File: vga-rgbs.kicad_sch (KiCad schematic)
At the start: 14 parts, among them J1 VGA, Q1 BC847, Q2 BC847, U1 74LS86

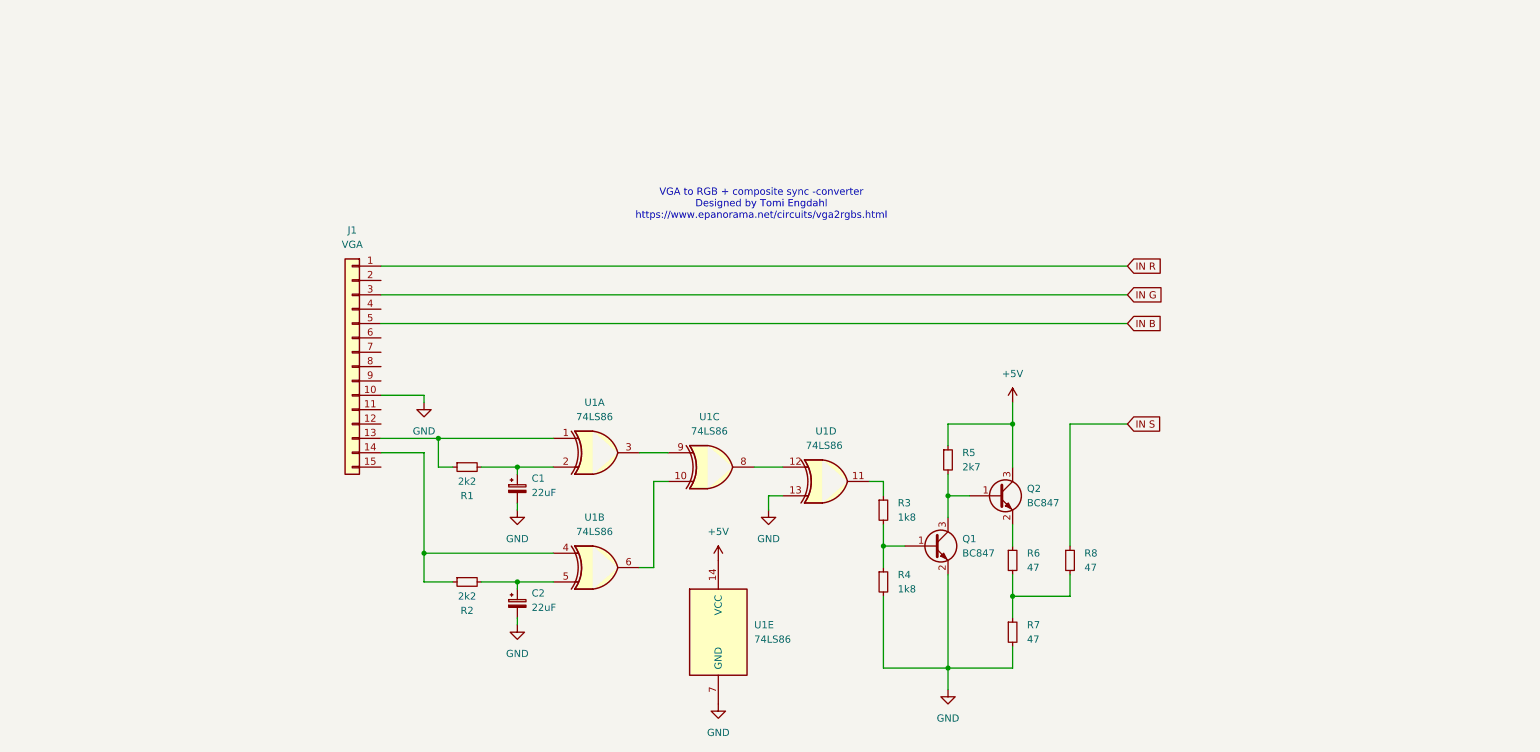
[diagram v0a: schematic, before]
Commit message: second design for nec tv and with inputs integrated
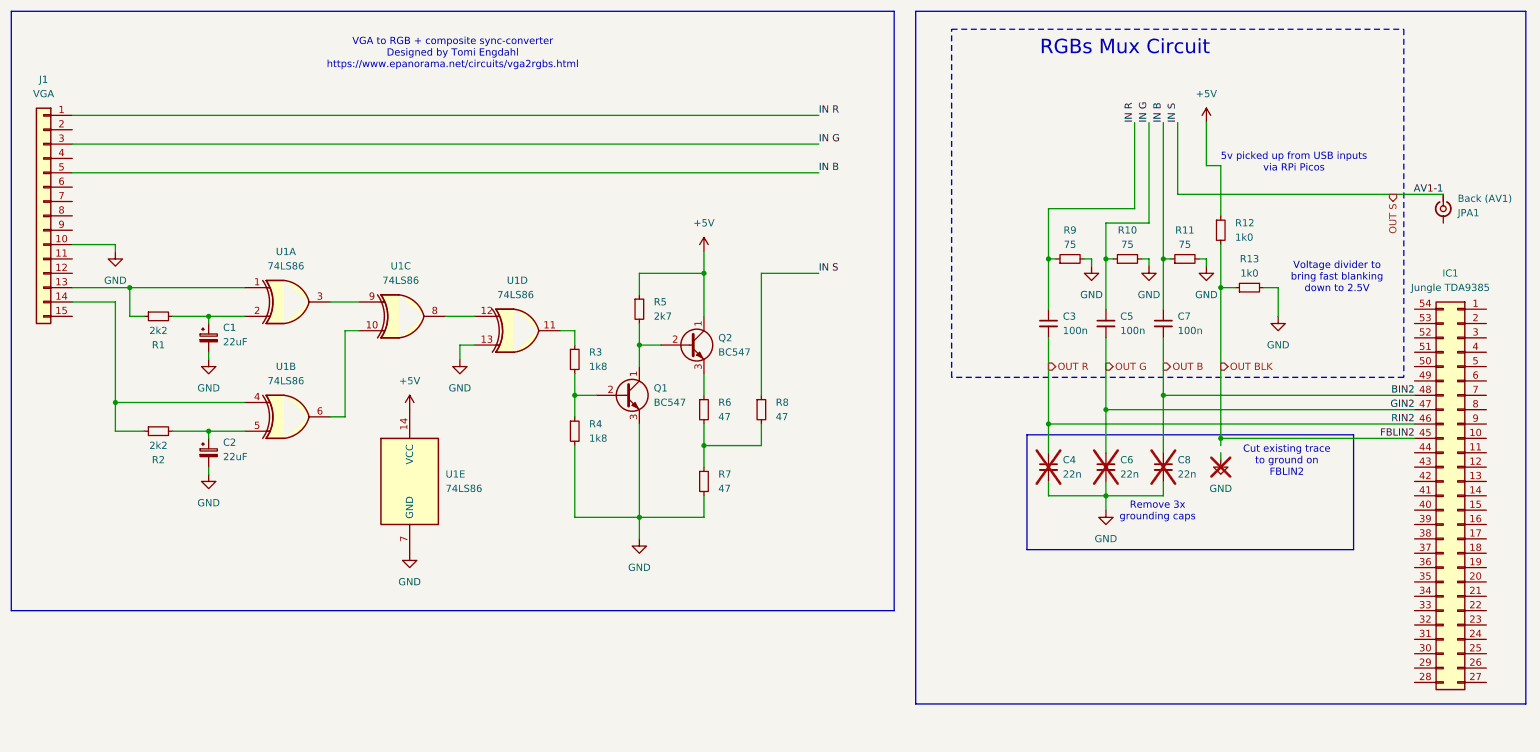
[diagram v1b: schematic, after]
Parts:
- removed Q1, Q2: BC847, Package_TO_SOT_THT:TO-92_Inline_Wide, symbol Transistor_BJT:BC847
- added C3, C5, C7: 100n, Capacitor_THT:C_Disc_D6.0mm_W2.5mm_P5.00mm, symbol Device:C_Small
- added C4, C6, C8: 22n, Capacitor_THT:C_Disc_D6.0mm_W2.5mm_P5.00mm, symbol Device:C_Small
- added IC1: Jungle TDA9385, symbol Connector_Generic:Conn_02x27_Counter_Clockwise
- added JPA1: Back (AV1), symbol Connector:Conn_Coaxial_Small
- added Q1, Q2: BC547, Package_TO_SOT_THT:TO-92_Inline, symbol Transistor_BJT:BC547
- added R10, R11, R9: 75, Resistor_THT:R_Axial_DIN0204_L3.6mm_D1.6mm_P7.62mm_Horizontal, symbol Device:R_Small
- added R12, R13: 1k0, Resistor_THT:R_Axial_DIN0204_L3.6mm_D1.6mm_P7.62mm_Horizontal, symbol Device:R_Small
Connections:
- net +5V: now also Q2.1 (C), R12.1
- net GND: now also C4.2, C6.2, C8.2, Q1.3 (E), R10.2, R11.2, R13.2, R9.2
- net IN B: now also C7.1, R11.1
- net IN G: now also C5.1, R10.1
- net IN R: now also C3.1, R9.1
- net at R3.2, R4.1: now also Q1.2 (B)
- net at R5.2: now also Q1.1 (C), Q2.2 (B)
- net at R6.1: now also Q2.3 (E)
- net IN S renamed OUT S
- net OUT S: now also JPA1.1 (In)
- new net OUT B: C7.2, C8.1, IC1.48 (Pin_48)
- new net OUT BLK: IC1.45 (Pin_45), R12.2, R13.1
- new net OUT G: C5.2, C6.1, IC1.47 (Pin_47)
- new net OUT R: C3.2, C4.1, IC1.46 (Pin_46)
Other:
- note added: "5v picked up from USB inputs via RPi Picos"
- note added: "Cut existing trace to ground on FBLIN2"
- note added: "RGBs Mux Circuit"
- note added: "Remove 3x grounding caps"
- note added: "VGA to RGB + composite sync-converter Designed by Tomi Engdahl https://www.epanorama.net/circuits/vga2rgbs.html"
- note added: "Voltage divider to bring fast blanking down to 2.5V"
- note removed: "VGA to RGB + composite sync -converter Designed by Tomi Engdahl https://www.epanorama.net/circuits/vga2rgbs.html"
- moved on the sheet: C1, C2, J1, R1, R2, R3, R4, R5, R6, R7, R8, U1A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
